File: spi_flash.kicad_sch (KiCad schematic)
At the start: 1 part, among them J2 ACA-SPI-004-K02

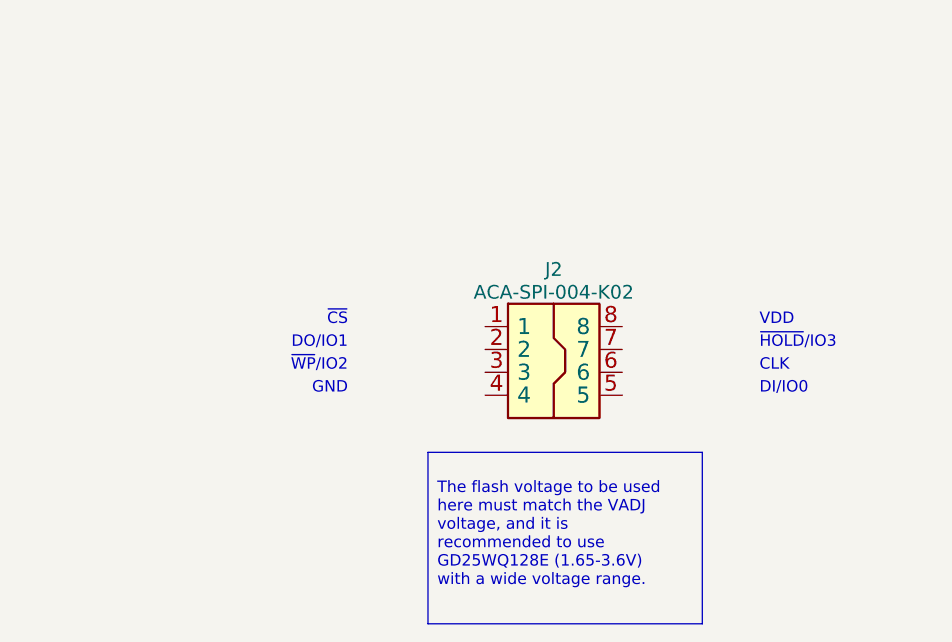
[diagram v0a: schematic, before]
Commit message: spi_flash.kicad_sch: finished spi flash schematic
Signed-off-by: Huang Rui <vowstar@gmail.com>
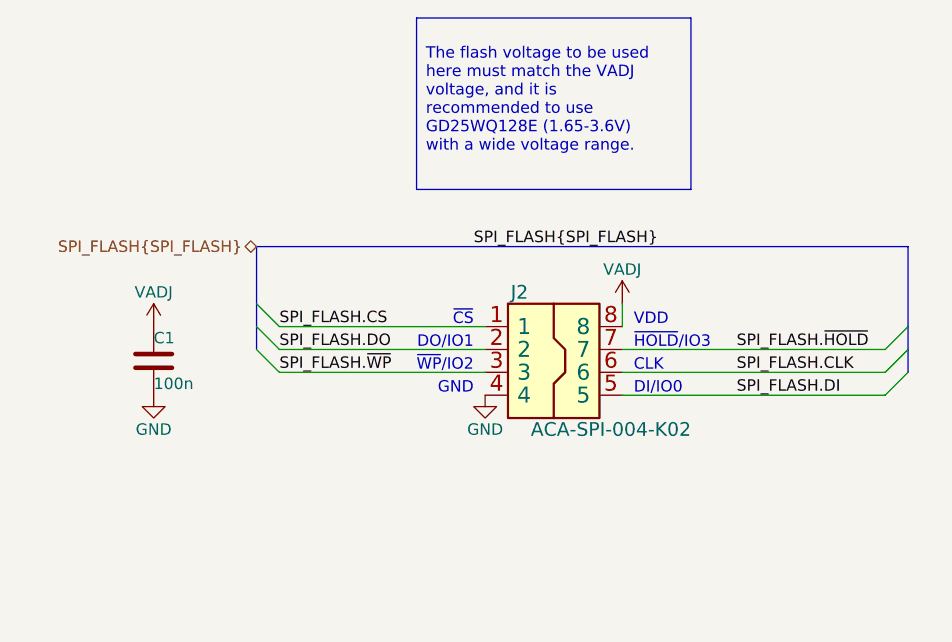
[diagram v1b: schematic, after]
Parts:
- added C1: 100n, Capacitor_SMD:C_0402_1005Metric, symbol Device:C
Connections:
- net SPI_FLASH.CS: now reaches J2.1
- net SPI_FLASH.DO: now reaches J2.2
- net SPI_FLASH.~{WP}: now reaches J2.3
- net GND: now reaches J2.4
- net GND: now also C1.2
- net SPI_FLASH.DI: now reaches J2.5
- net SPI_FLASH.CLK: now reaches J2.6
- net SPI_FLASH.~{HOLD}: now reaches J2.7
- net VDD: now reaches J2.8
- net VDD: now also C1.1

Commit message: *.kicad_sch: add CHIPSAlliance_ prefix for footprint
Signed-off-by: Huang Rui <vowstar@gmail.com>
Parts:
- J2: footprint Connector:ACA-SPI-004 -> CHIPSAlliance_Connector:ACA-SPI-004
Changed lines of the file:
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@@
       (effects (font (size 1.524 1.524)))
     )
-    (property "Footprint" "Connector:ACA-SPI-004" (at 114.3 119.38 0)
+    (property "Footprint" "CHIPSAlliance_Connector:ACA-SPI-004" (at 114.3 119.38 0)
       (effects (font (size 1.524 1.524)) (justify left) hide)
     )

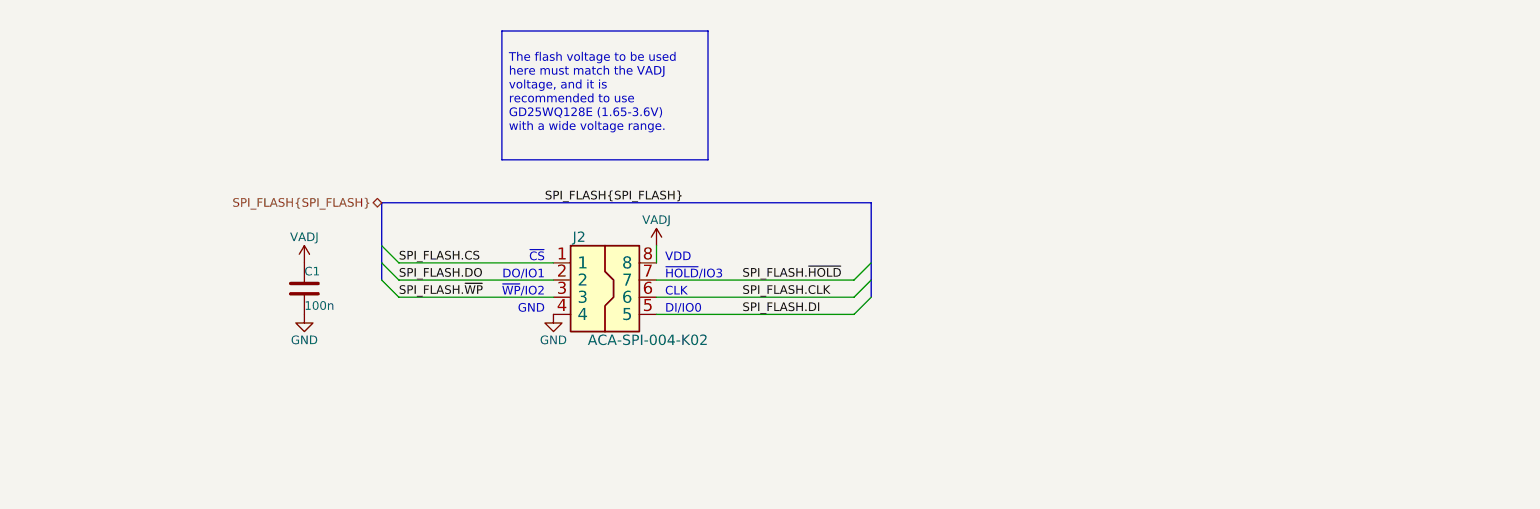
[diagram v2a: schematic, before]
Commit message: {spi,uart,usb}.kicad_sch: add TPD4E02B04DQA as ESD protect
Signed-off-by: Huang Rui <vowstar@gmail.com>
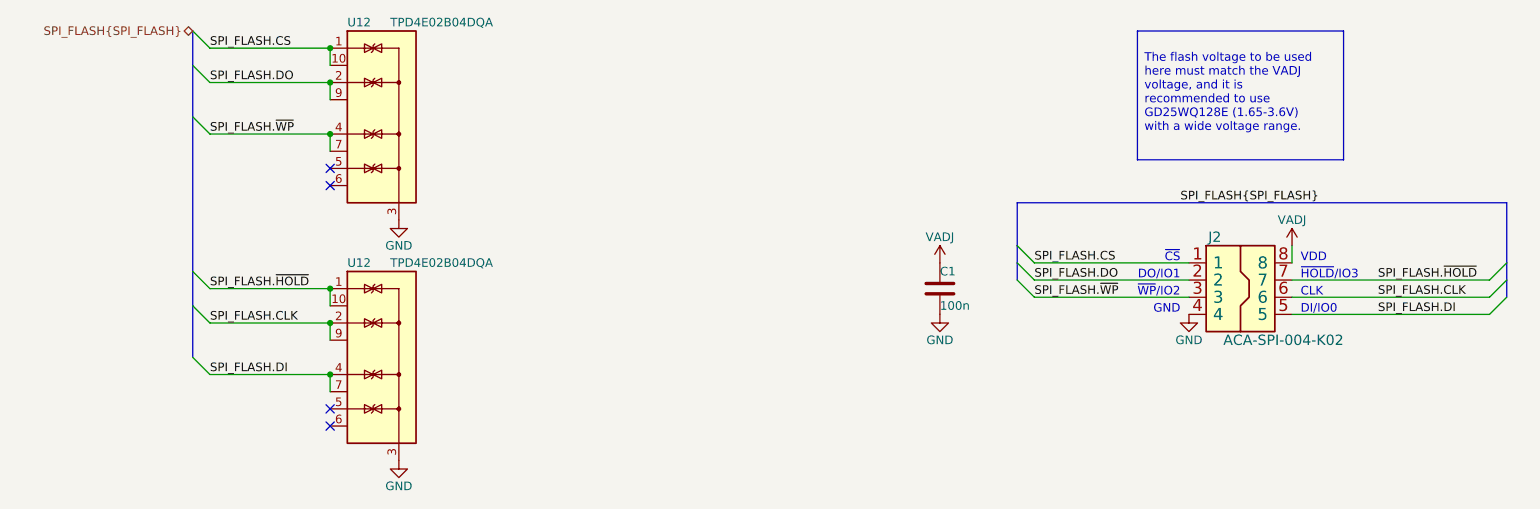
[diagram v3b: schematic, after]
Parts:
- added U12 (x2): TPD4E02B04DQA, Package_SON:USON-10_2.5x1.0mm_P0.5mm, symbol Power_Protection:TPD4E02B04DQA
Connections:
- net GND: now also U12.3 (G), U12.3 (G), U12.8 (G), U12.8 (G)
- net SPI_FLASH.CLK: now also U12.2 (IO2), U12.9 (NC)
- net SPI_FLASH.CS: now also U12.1 (IO1), U12.10 (NC)
- net SPI_FLASH.DI: now also U12.4 (IO3), U12.7 (NC)
- net SPI_FLASH.DO: now also U12.2 (IO2), U12.9 (NC)
- net SPI_FLASH.~{HOLD}: now also U12.1 (IO1), U12.10 (NC)
- net SPI_FLASH.~{WP}: now also U12.4 (IO3), U12.7 (NC)
- no-connect marks 0 -> 4
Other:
- moved on the sheet: C1, J2
